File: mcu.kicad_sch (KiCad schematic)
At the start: 16 parts, among them J1 STLink, SW1 SW_Push, SW2 SW_Push, U1 STM32G431CBTx, Y1 Resonator

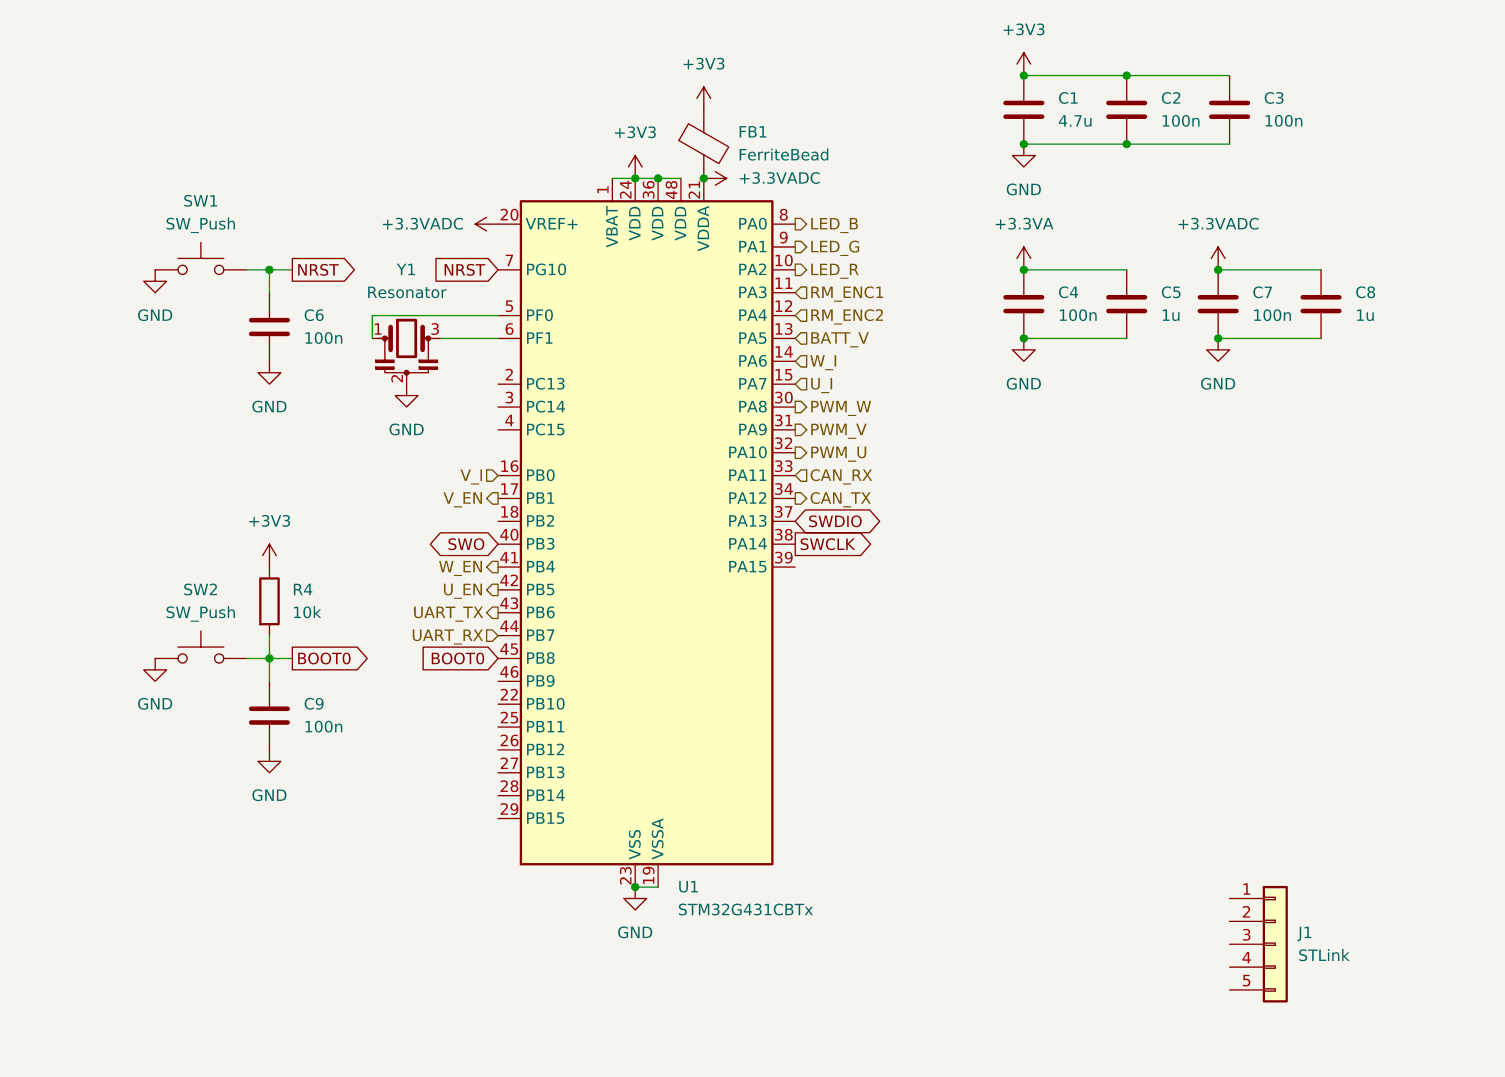
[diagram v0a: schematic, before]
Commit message: 回路図ほぼ完成 MOSFETのゲート抵抗の決め方よくわかんないです助けて
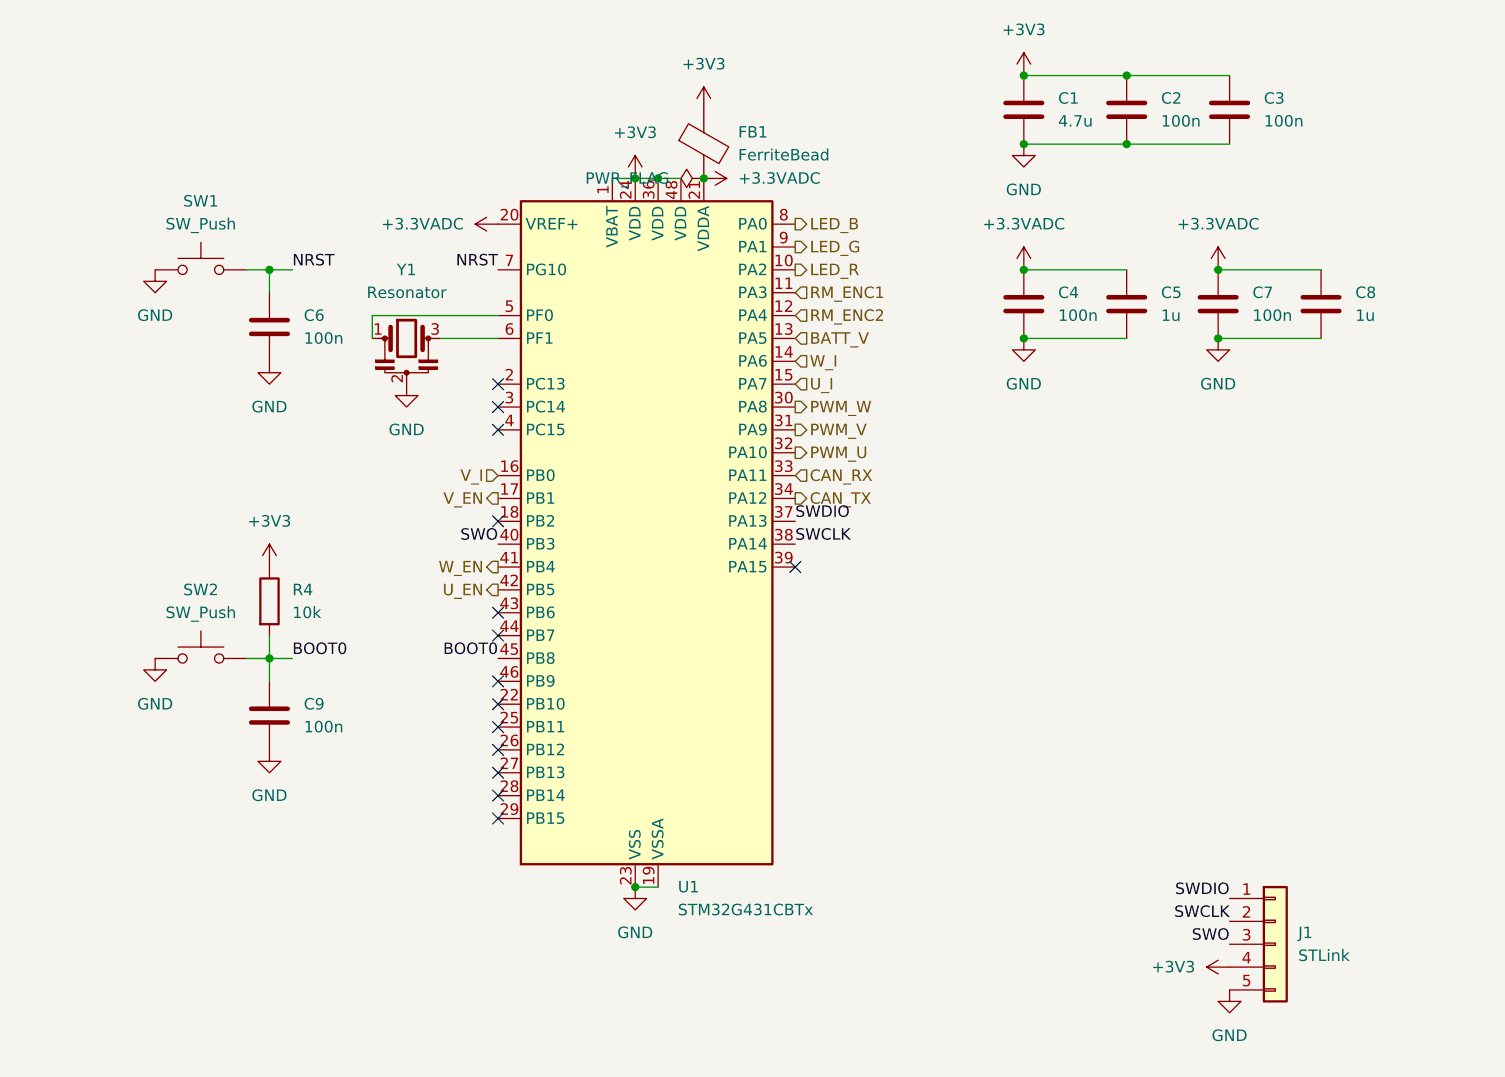
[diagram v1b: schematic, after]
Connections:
- net +3.3VA is gone; now on net +3.3VADC: C4.1, C5.1
- net +3V3: now also J1.4 (Pin_4)
- net GND: now also J1.5 (Pin_5)
- net SWCLK: now also J1.2 (Pin_2)
- net SWDIO: now also J1.1 (Pin_1)
- net SWO: now also J1.3 (Pin_3)
- net UART_RX: no longer names the net of U1.44 (PB7)
- net UART_TX: no longer names the net of U1.43 (PB6)
- no-connect marks 0 -> 14
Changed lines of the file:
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@@
   (junction (at 95.25 41.91) (diameter 0) (color 0 0 0 0)
   )
+  (junction (at 138.43 52.07) (diameter 0) (color 0 0 0 0)
+  )
   (junction (at 138.43 38.1) (diameter 0) (color 0 0 0 0)
   )
-  (junction (at 138.43 52.07) (diameter 0) (color 0 0 0 0)
-  )
   (junction (at 95.25 120.65) (diameter 0) (color 0 0 0 0)
   )
@@
   (junction (at 54.61 52.07) (diameter 0) (color 0 0 0 0)
   )
+  (no_connect (at 80.01 69.85))
+  (no_connect (at 80.01 64.77))
+  (no_connect (at 80.01 92.71))
+  (no_connect (at 80.01 107.95))
+  (no_connect (at 80.01 97.79))
+  (no_connect (at 80.01 100.33))
+  (no_connect (at 80.01 67.31))
+  (no_connect (at 80.01 105.41))
+  (no_connect (at 80.01 110.49))
+  (no_connect (at 80.01 80.01))
+  (no_connect (at 113.03 85.09))
+  (no_connect (at 80.01 113.03))
+  (no_connect (at 80.01 90.17))
+  (no_connect (at 80.01 102.87))
   (wire (pts (xy 54.61 52.07) (xy 54.61 54.61))
     (stroke (width 0) (type default))
@@
     (stroke (width 0) (type default))
   )
-  (global_label "NRST" (shape output) (at 57.15 52.07 0) (fields_autoplaced)
-    (effects (font (size 1.27 1.27)) (justify left))
-    (property "Intersheetrefs" "${INTERSHEET_REFS}" (at 64.9128 52.07 0)
-      (effects (font (size 1.27 1.27)) (justify left) hide)
-    )
-  )
-  (global_label "SWO" (shape bidirectional) (at 80.01 82.55 180) (fields_autoplaced)
-    (effects (font (size 1.27 1.27)) (justify right))
-    (property "Intersheetrefs" "${INTERSHEET_REFS}" (at 71.9221 82.55 0)
-      (effects (font (size 1.27 1.27)) (justify right) hide)
-    )
-  )
-  (global_label "BOOT0" (shape input) (at 80.01 95.25 180) (fields_autoplaced)
-    (effects (font (size 1.27 1.27)) (justify right))
-    (property "Intersheetrefs" "${INTERSHEET_REFS}" (at 70.9167 95.25 0)
-      (effects (font (size 1.27 1.27)) (justify right) hide)
-    )
-  )
-  (global_label "NRST" (shape input) (at 80.01 52.07 180) (fields_autoplaced)
-    (effects (font (size 1.27 1.27)) (justify right))
-    (property "Intersheetrefs" "${INTERSHEET_REFS}" (at 72.2472 52.07 0)
-      (effects (font (size 1.27 1.27)) (justify right) hide)
-    )
-  )
-  (global_label "SWCLK" (shape output) (at 113.03 82.55 0) (fields_autoplaced)
-    (effects (font (size 1.27 1.27)) (justify left))
-    (property "Intersheetrefs" "${INTERSHEET_REFS}" (at 122.2442 82.55 0)
-      (effects (font (size 1.27 1.27)) (justify left) hide)
-    )
-  )
-  (global_label "SWDIO" (shape bidirectional) (at 113.03 80.01 0) (fields_autoplaced)
-    (effects (font (size 1.27 1.27)) (justify left))
-    (property "Intersheetrefs" "${INTERSHEET_REFS}" (at 122.9927 80.01 0)
-      (effects (font (size 1.27 1.27)) (justify left) hide)
-    )
-  )
-  (global_label "BOOT0" (shape output) (at 57.15 95.25 0) (fields_autoplaced)
-    (effects (font (size 1.27 1.27)) (justify left))
-    (property "Intersheetrefs" "${INTERSHEET_REFS}" (at 66.2433 95.25 0)
-      (effects (font (size 1.27 1.27)) (justify left) hide)
-    )
+  (label "SWCLK" (at 113.03 82.55 0) (fields_autoplaced)
+    (effects (font (size 1.27 1.27)) (justify left bottom))
+  )
+  (label "SWO" (at 161.29 127 180) (fields_autoplaced)
+    (effects (font (size 1.27 1.27)) (justify right bottom))
+  )
+  (label "SWO" (at 80.01 82.55 180) (fields_autoplaced)
+    (effects (font (size 1.27 1.27)) (justify right bottom))
+  )
+  (label "NRST" (at 80.01 52.07 180) (fields_autoplaced)
+    (effects (font (size 1.27 1.27)) (justify right bottom))
+  )
+  (label "SWDIO" (at 113.03 80.01 0) (fields_autoplaced)
+    (effects (font (size 1.27 1.27)) (justify left bottom))
+  )
+  (label "SWCLK" (at 161.29 124.46 180) (fields_autoplaced)
+    (effects (font (size 1.27 1.27)) (justify right bottom))
+  )
+  (label "BOOT0" (at 57.15 95.25 0) (fields_autoplaced)
+    (effects (font (size 1.27 1.27)) (justify left bottom))
+  )
+  (label "SWDIO" (at 161.29 121.92 180) (fields_autoplaced)
+    (effects (font (size 1.27 1.27)) (justify right bottom))
+  )
+  (label "NRST" (at 57.15 52.07 0) (fields_autoplaced)
+    (effects (font (size 1.27 1.27)) (justify left bottom))
+  )
+  (label "BOOT0" (at 80.01 95.25 180) (fields_autoplaced)
+    (effects (font (size 1.27 1.27)) (justify right bottom))
   )
   (hierarchical_label "LED_B" (shape output) (at 113.03 46.99 0) (fields_autoplaced)
@@
   (hierarchical_label "RM_ENC2" (shape input) (at 113.03 57.15 0) (fields_autoplaced)
     (effects (font (size 1.27 1.27)) (justify left))
-  )
-  (hierarchical_label "UART_TX" (shape output) (at 80.01 90.17 180) (fields_autoplaced)
-    (effects (font (size 1.27 1.27)) (justify right))
   )
   (hierarchical_label "LED_G" (shape output) (at 113.03 49.53 0) (fields_autoplaced)
@@
     (effects (font (size 1.27 1.27)) (justify left))
   )
-  (hierarchical_label "UART_RX" (shape input) (at 80.01 92.71 180) (fields_autoplaced)
-    (effects (font (size 1.27 1.27)) (justify right))
-  )
   (hierarchical_label "U_I" (shape input) (at 113.03 64.77 0) (fields_autoplaced)
     (effects (font (size 1.27 1.27)) (justify left))
@@
         (path "/181c0b55-802a-4742-8349-1028710992a0/9de6f89a-6a03-4303-bc89-6d3e81c44499"
           (reference "FB1") (unit 1)
+        )
+      )
+    )
+  )
+  (symbol (lib_id "power:+3V3") (at 161.29 129.54 90) (unit 1)
+    (in_bom yes) (on_board yes) (dnp no) (fields_autoplaced)
+    (property "Reference" "#PWR086" (at 165.1 129.54 0)
+      (effects (font (size 1.27 1.27)) hide)
+    )
+    (property "Value" "+3V3" (at 157.48 129.54 90)
+      (effects (font (size 1.27 1.27)) (justify left))
+    )
+    (property "Footprint" "" (at 161.29 129.54 0)
+      (effects (font (size 1.27 1.27)) hide)
+    )
+    (property "Datasheet" "" (at 161.29 129.54 0)
+      (effects (font (size 1.27 1.27)) hide)
+    )
+    (pin "1")
+    (instances
+      (project "blmd_hardware"
+        (path "/181c0b55-802a-4742-8349-1028710992a0/9de6f89a-6a03-4303-bc89-6d3e81c44499"
+          (reference "#PWR086") (unit 1)
         )
       )
@@
     )
   )
+  (symbol (lib_id "power:PWR_FLAG") (at 102.87 41.91 90) (unit 1)
+    (in_bom yes) (on_board yes) (dnp no) (fields_autoplaced)
+    (property "Reference" "#FLG06" (at 100.965 41.91 0)
+      (effects (font (size 1.27 1.27)) hide)
+    )
+    (property "Value" "PWR_FLAG" (at 99.06 41.91 90)
+      (effects (font (size 1.27 1.27)) (justify left))
+    )
+    (property "Footprint" "" (at 102.87 41.91 0)
+      (effects (font (size 1.27 1.27)) hide)
+    )
+    (property "Datasheet" "~" (at 102.87 41.91 0)
+      (effects (font (size 1.27 1.27)) hide)
+    )
+    (pin "1")
+    (instances
+      (project "blmd_hardware"
+        (path "/181c0b55-802a-4742-8349-1028710992a0/9de6f89a-6a03-4303-bc89-6d3e81c44499"
+          (reference "#FLG06") (unit 1)
+        )
+      )
+    )
+  )
   (symbol (lib_id "power:GND") (at 138.43 38.1 0) (unit 1)
     (in_bom yes) (on_board yes) (dnp no) (fields_autoplaced)
@@
         (path "/181c0b55-802a-4742-8349-1028710992a0/9de6f89a-6a03-4303-bc89-6d3e81c44499"
           (reference "C2") (unit 1)
+        )
+      )
+    )
+  )
+  (symbol (lib_id "power:+3.3VADC") (at 138.43 52.07 0) (unit 1)
+    (in_bom yes) (on_board yes) (dnp no) (fields_autoplaced)
+    (property "Reference" "#PWR079" (at 142.24 53.34 0)
+      (effects (font (size 1.27 1.27)) hide)
+    )
+    (property "Value" "+3.3VADC" (at 138.43 46.99 0)
+      (effects (font (size 1.27 1.27)))
+    )
+    (property "Footprint" "" (at 138.43 52.07 0)
+      (effects (font (size 1.27 1.27)) hide)
+    )
+    (property "Datasheet" "" (at 138.43 52.07 0)
+      (effects (font (size 1.27 1.27)) hide)
+    )
+    (pin "1")
+    (instances
+      (project "blmd_hardware"
+        (path "/181c0b55-802a-4742-8349-1028710992a0/9de6f89a-6a03-4303-bc89-6d3e81c44499"
+          (reference "#PWR079") (unit 1)
         )
       )
@@
     )
   )
-  (symbol (lib_id "power:+3.3VA") (at 138.43 52.07 0) (unit 1)
-    (in_bom yes) (on_board yes) (dnp no) (fields_autoplaced)
-    (property "Reference" "#PWR011" (at 138.43 55.88 0)
-      (effects (font (size 1.27 1.27)) hide)
-    )
-    (property "Value" "+3.3VA" (at 138.43 46.99 0)
-      (effects (font (size 1.27 1.27)))
-    )
-    (property "Footprint" "" (at 138.43 52.07 0)
-      (effects (font (size 1.27 1.27)) hide)
-    )
-    (property "Datasheet" "" (at 138.43 52.07 0)
-      (effects (font (size 1.27 1.27)) hide)
-    )
-    (pin "1")
-    (instances
-      (project "blmd_hardware"
-        (path "/181c0b55-802a-4742-8349-1028710992a0/9de6f89a-6a03-4303-bc89-6d3e81c44499"
-          (reference "#PWR011") (unit 1)
-        )
-      )
-    )
-  )
   (symbol (lib_id "power:+3V3") (at 102.87 34.29 0) (unit 1)
     (in_bom yes) (on_board yes) (dnp no) (fields_autoplaced)
@@
         )
       )
+    )
+  )
+  (symbol (lib_id "power:GND") (at 161.29 132.08 0) (unit 1)
+    (in_bom yes) (on_board yes) (dnp no) (fields_autoplaced)
+    (property "Reference" "#PWR087" (at 161.29 138.43 0)
+      (effects (font (size 1.27 1.27)) hide)
+    )
+    (property "Value" "GND" (at 161.29 137.16 0)
+      (effects (font (size 1.27 1.27)))
+    )
+    (property "Footprint" "" (at 161.29 132.08 0)
+      (effects (font (size 1.27 1.27)) hide)
+    )
+    (property "Datasheet" "" (at 161.29 132.08 0)
+      (effects (font (size 1.27 1.27)) hide)
+    )
+    (pin "1")
+    (instances
+      (project "blmd_hardware"
+        (path "/181c0b55-802a-4742-8349-1028710992a0/9de6f89a-6a03-4303-bc89-6d3e81c44499"
+          (reference "#PWR087") (unit 1)
+        )
+      )

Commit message: 部品配置完了(暫定)
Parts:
- removed C9: 100n, symbol Device:C
- removed J1: STLink, symbol Connector_Generic:Conn_01x05
- removed SW2: SW_Push, symbol Switch:SW_Push
- removed Y1: Resonator, symbol Device:Resonator
- added J1: Conn_02x07_Odd_Even, Connector_PinHeader_1.27mm:PinHeader_2x07_P1.27mm_Vertical, symbol Connector_Generic:Conn_02x07_Odd_Even
- added R13, R14, R15, R16: 10k, Resistor_SMD:R_0603_1608Metric_Pad0.98x0.95mm_HandSolder, symbol Device:R
- added R20: 100, Resistor_SMD:R_0603_1608Metric_Pad0.98x0.95mm_HandSolder, symbol Device:R
- added SW2: SW_DIP_x04, Button_Switch_SMD:SW_DIP_SPSTx04_Slide_Copal_CHS-04B_W7.62mm_P1.27mm, symbol Switch:SW_DIP_x04
- C1, C2, C3, C4, C5, C6, C7, C8, FB1: footprint (none) -> Capacitor_SMD:C_0603_1608Metric_Pad1.08x0.95mm_HandSolder
- R4: footprint (none) -> Resistor_SMD:R_0603_1608Metric_Pad0.98x0.95mm_HandSolder
- SW1: footprint (none) -> d_robo_lib:TVAF06-A020B-R
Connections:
- net +3V3: now also J1.3 (Pin_3), R13.1, R14.1, R15.1, R16.1; no longer R4.1
- net GND: now also R4.1, J1.5 (Pin_5), J1.7 (Pin_7), R20.1, SW2.5, SW2.6, SW2.7, SW2.8
- net NRST: now also J1.12 (Pin_12)
- net SWCLK: now also J1.6 (Pin_6)
- net SWDIO: now also J1.4 (Pin_4)
- net SWO: now also J1.8 (Pin_8)
- net MODE1: now reaches U1.25 (PB11)
- net MODE1: now also R13.2, SW2.1
- net MODE2: now reaches U1.26 (PB12)
- net MODE2: now also R14.2, SW2.2
- net MODE3: now reaches U1.27 (PB13)
- net MODE3: now also R15.2, SW2.3
- net MODE4: now reaches U1.28 (PB14)
- net MODE4: now also R16.2, SW2.4
- net UART_TX: now reaches U1.43 (PB6)
- net UART_TX: now also J1.13 (Pin_13)
- net UART_RX: now reaches U1.44 (PB7)
- net UART_RX: now also J1.14 (Pin_14)
- new net: J1.11 (Pin_11), R20.2
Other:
- moved on the sheet: R4
